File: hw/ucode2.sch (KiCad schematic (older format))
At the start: 16 parts, among them U801 74HC00, U802 74HC590, U803 27C64, U804 27C64, U805 27C64, U806 27C64, U807 74HCT175, U808 74HCT175, U809 74HCT175, U810 74HCT175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

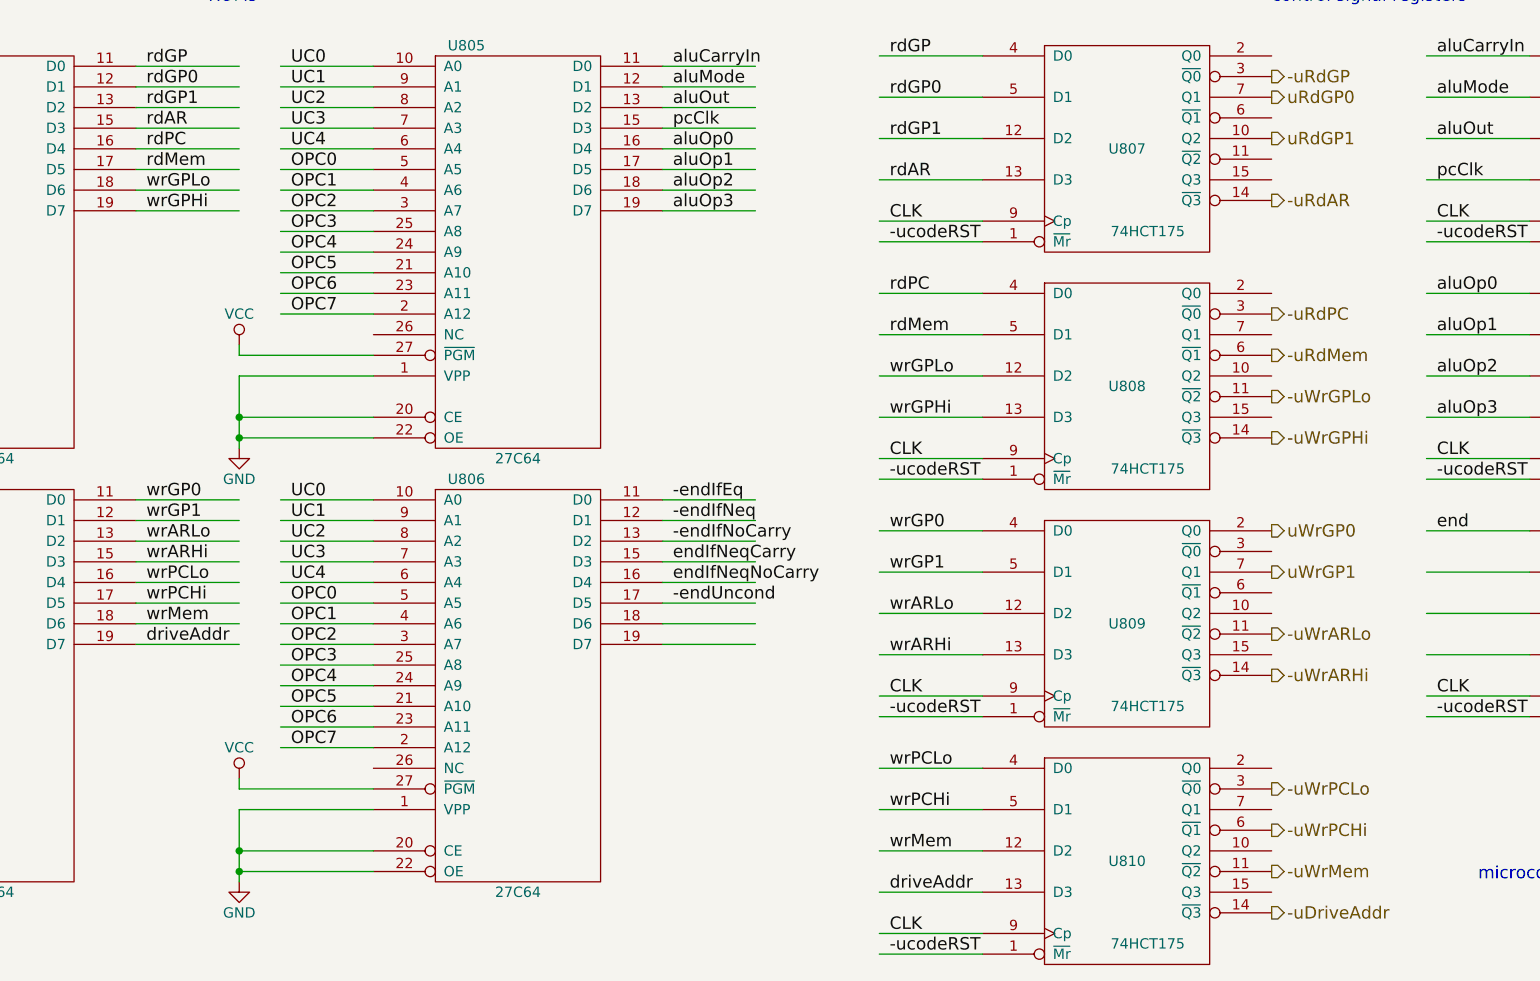
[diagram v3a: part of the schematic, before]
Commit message: added bus/address register module
Used a '245 bus transceiver to do reads from
and writes to the external data bus, so the
control signals for reading and writing memory
changed (to -rwMem and memDir, rather than
separate read and write signals.)

At this point, I think all of the required modules
are in place, although not all of the connections are
shown on the top-level schematic.
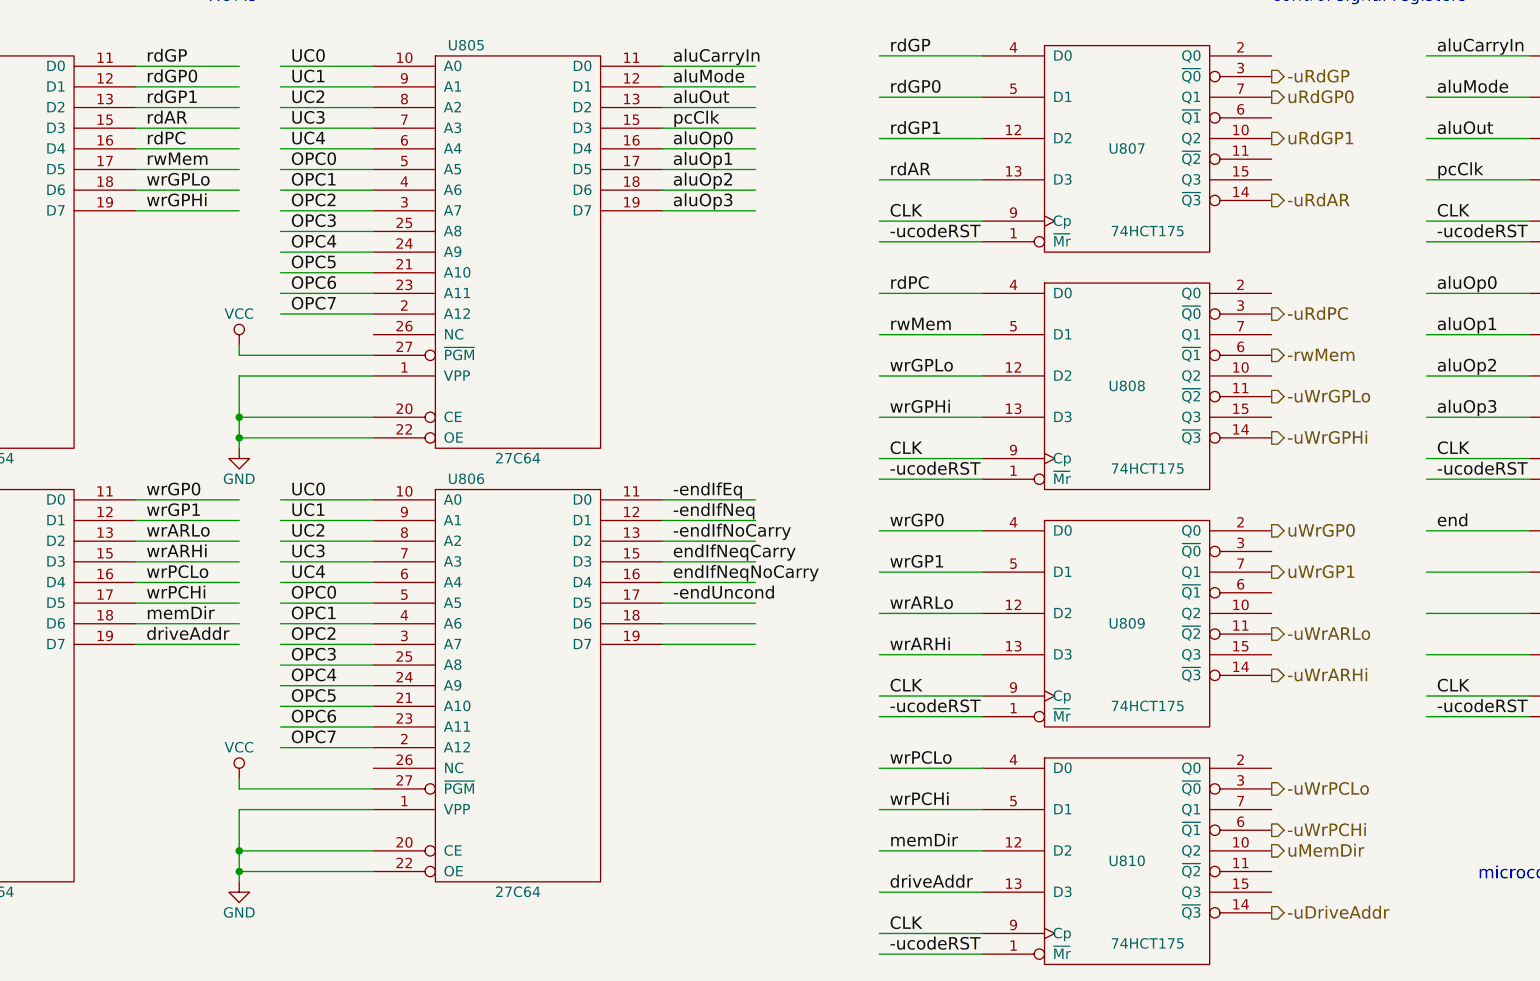
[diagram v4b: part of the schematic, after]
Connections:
- net labels added: -rwMem, memDir, rwMem, uMemDir
- net labels removed: -uRdMem, -uWrMem, rdMem, wrMem
- wire segments 246 -> 245

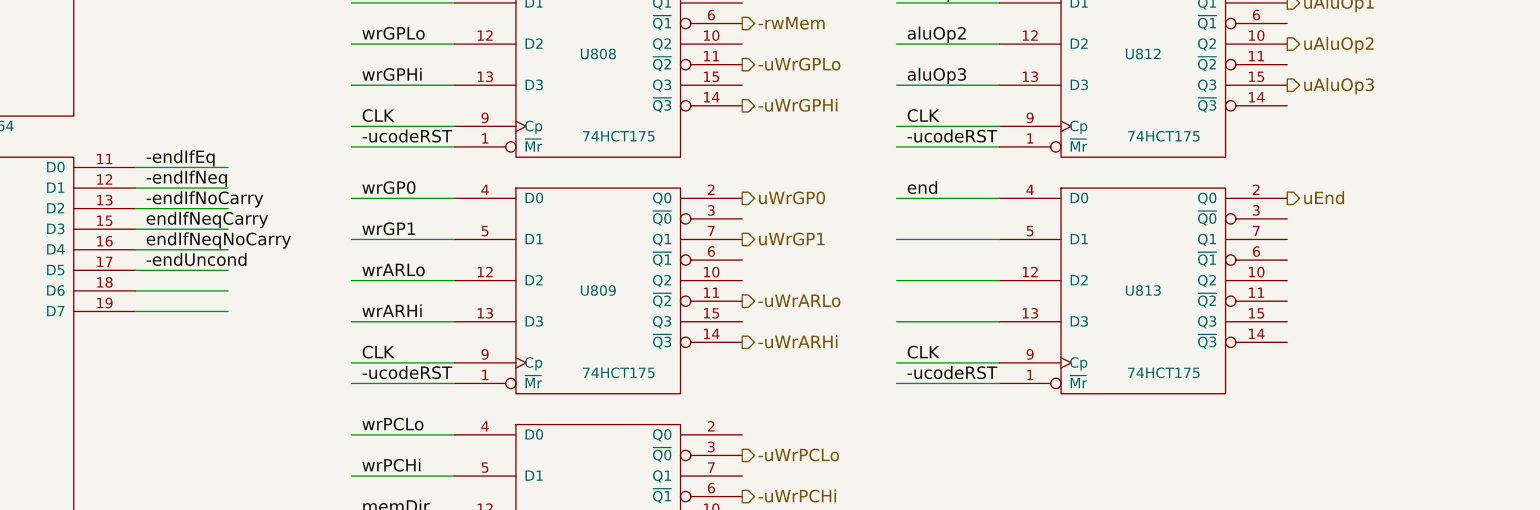
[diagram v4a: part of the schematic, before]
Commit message: use '573 latches as address bus drivers
This let's us latch the address being asserted onto
the left/right ALU inputs busses in case it is going
to change during the execution of the instruction.
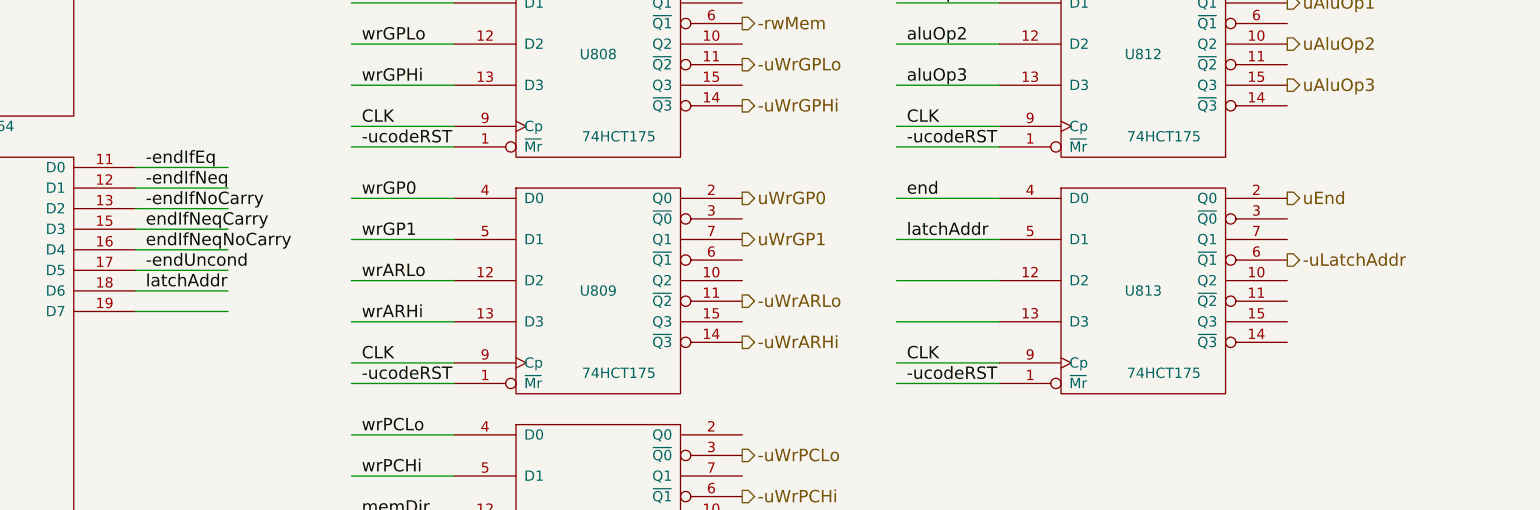
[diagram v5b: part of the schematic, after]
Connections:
- net labels added: -uLatchAddr, latchAddr
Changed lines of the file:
@@
 Text HLabel 8300 9000 2    60   Output ~ 0
 uMemDir
+Text Label 5400 7900 0    60   ~ 0
+latchAddr
+Text Label 9100 7650 0    60   ~ 0
+latchAddr
+Text HLabel 10950 7750 2    60   Output ~ 0
+-uLatchAddr
 $EndSCHEMATC

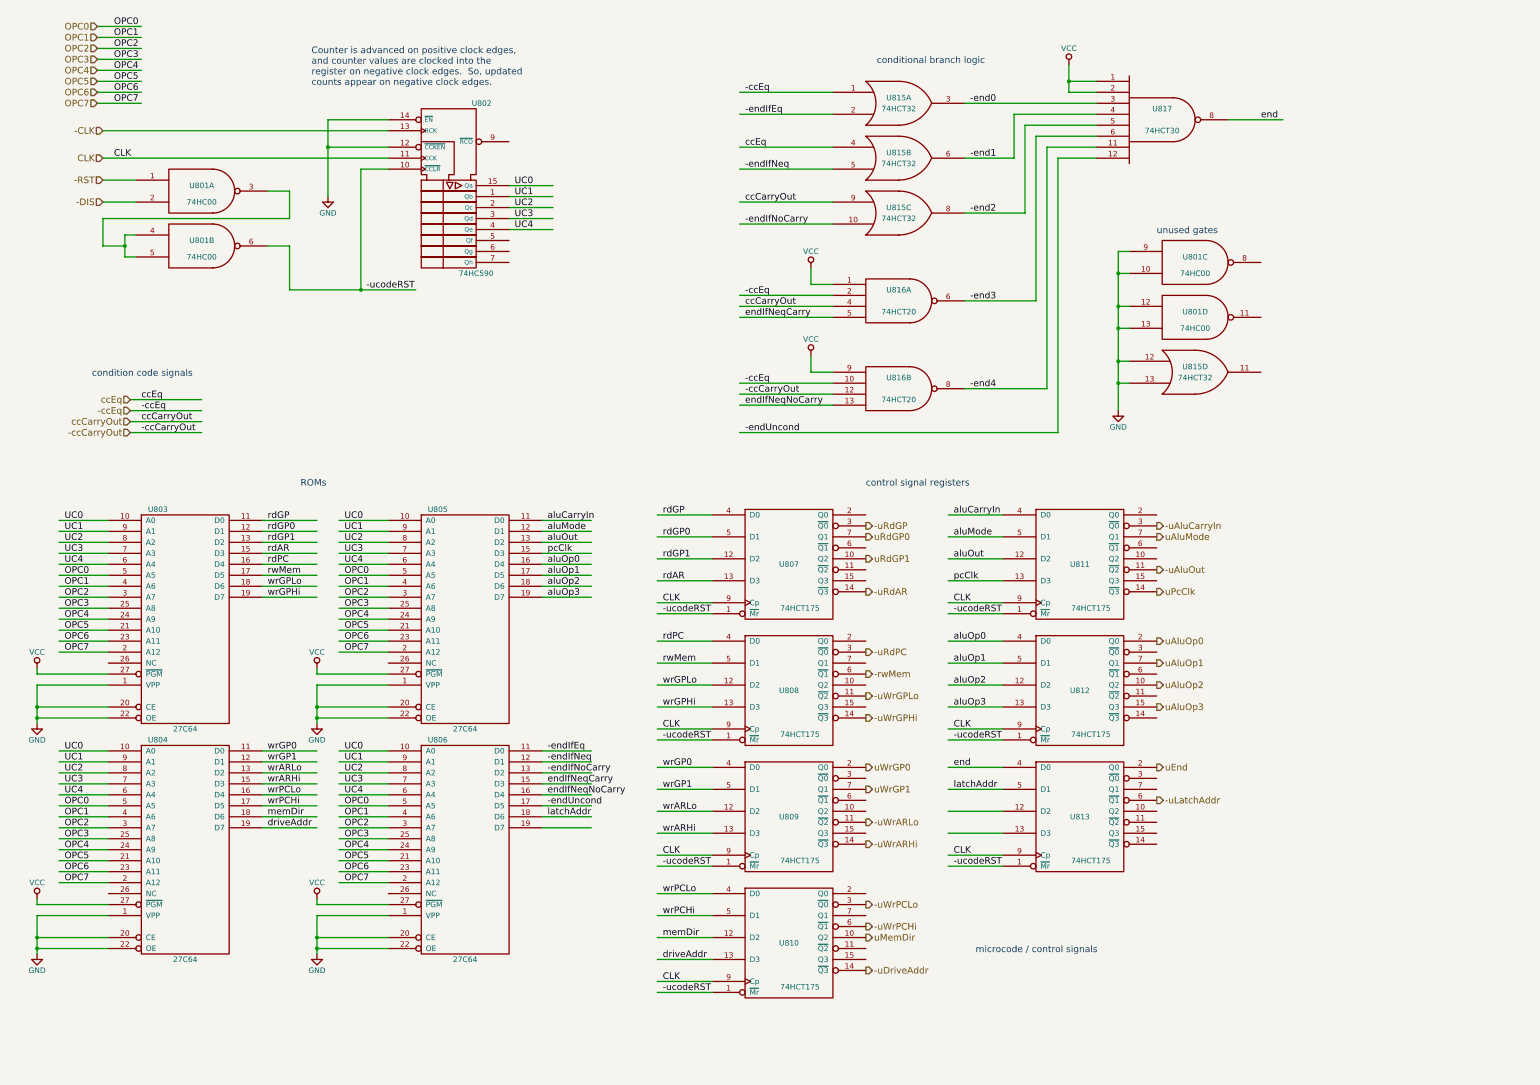
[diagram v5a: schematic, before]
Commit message: generate external r/w signals
Found a way to do this without increasing the chip
count: use NAND gates to produce some of the conditional
end signals (rather than OR gates), and use AND gates
to generate the -ucodeRST signal and the new
extW/extR signals.  These are active high, and
are generated as inverted, ensuring that the
final -uExtW and -uExtR signals are not asserted
on reset.
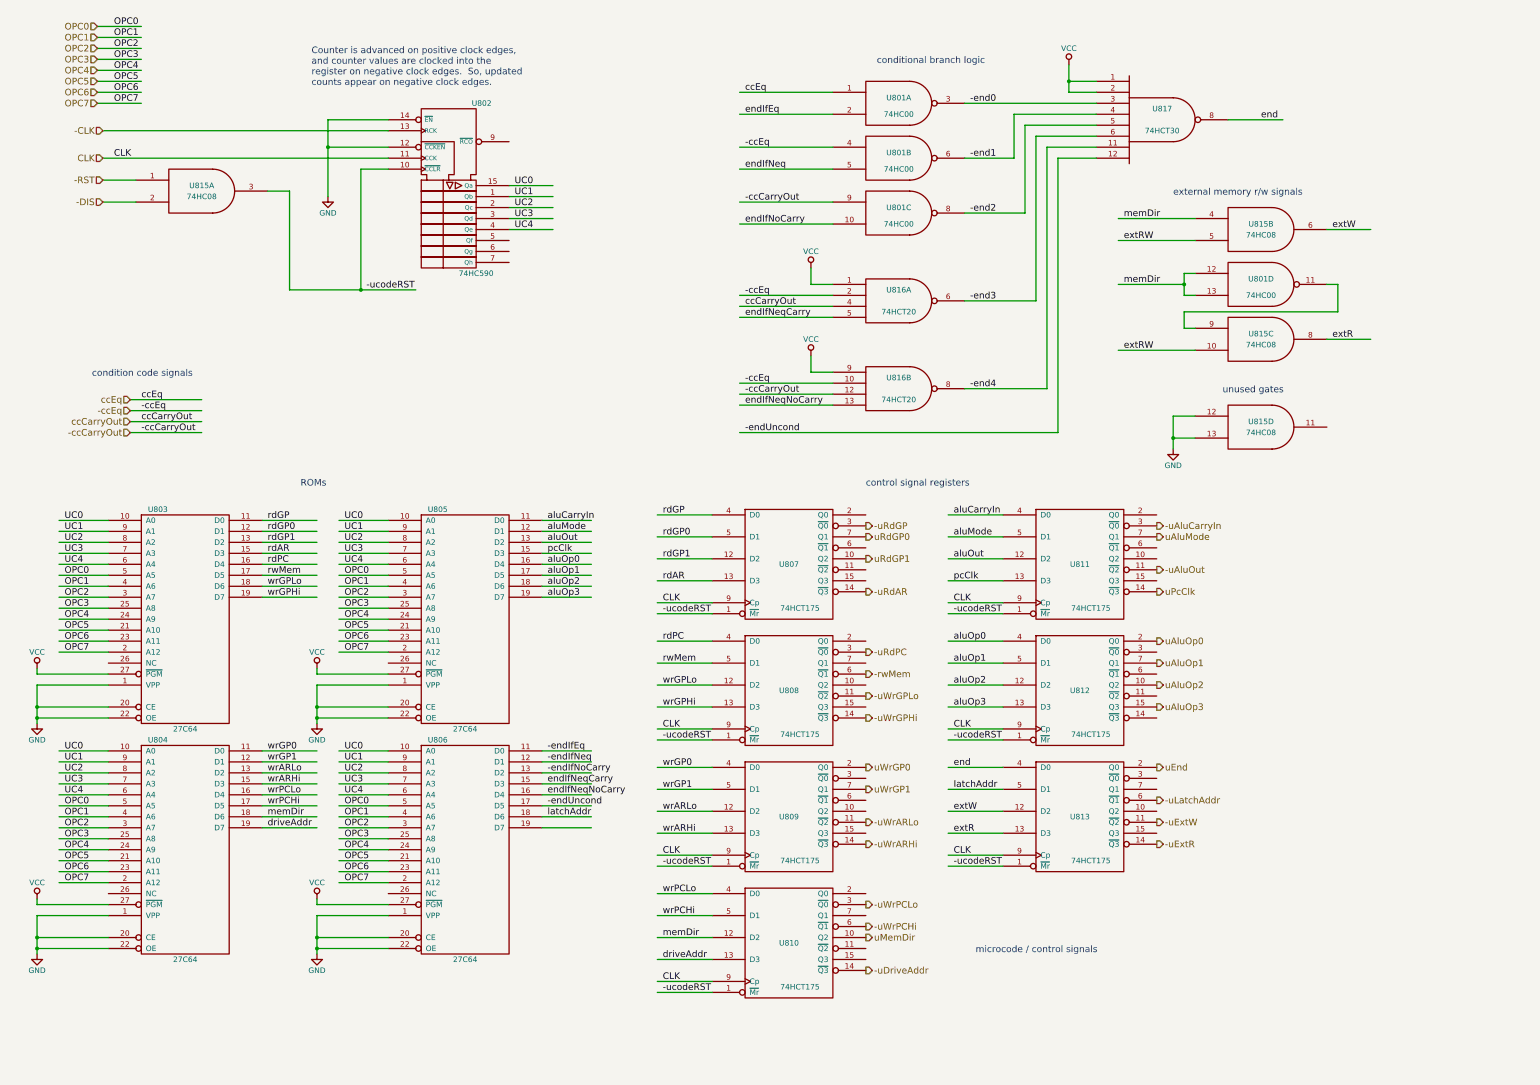
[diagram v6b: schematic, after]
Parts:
- removed U815: 74HCT32, symbol 74LS32
- added U815: 74HC08, symbol 74LS08
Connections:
- net labels added: -uExtR, -uExtW, endIfEq, endIfNeq, endIfNoCarry, extR, extRW, extW
- wire segments 245 -> 247
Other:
- note added: "external memory r/w signals"
- moved on the sheet: U801A, U801B, U801C, U801D
